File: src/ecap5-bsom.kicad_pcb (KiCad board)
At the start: 2 copper layers, 69.6 x 30 mm, 183 parts, among them J13 DDR4_SODIMM_Board, U1 L6981NDR, U10 IS42S16160J-*BL, U11 IS43DR86400E, U12 ASFC4G31M-51*, U2 L6981NDR, U3 ST1S41PHR, U4 L6981NDR, U5 LM3880MF*-1AA, U6 LFE5U-85F-*BG756*, U7 XLH335040.000000I, U8 W25Q128JVPIQ, U9 IS61WV25616BLL-*BLI

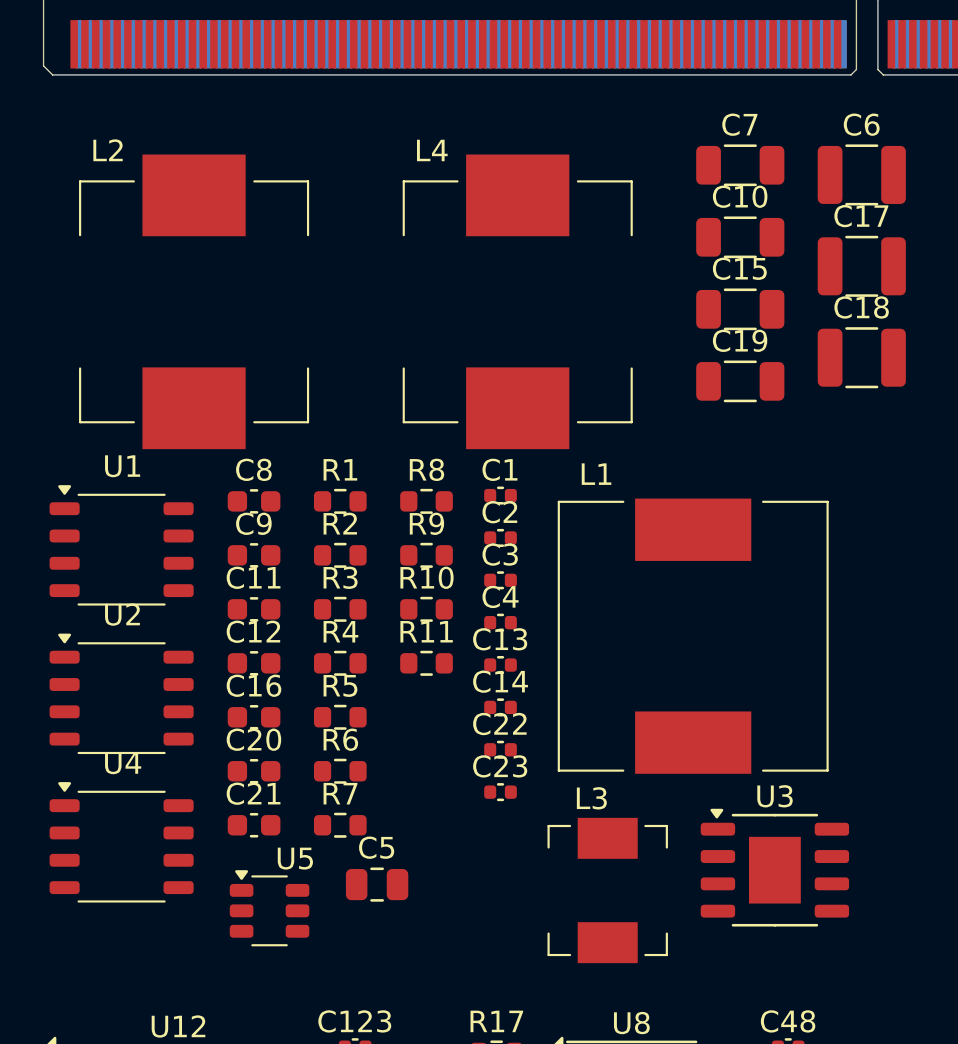
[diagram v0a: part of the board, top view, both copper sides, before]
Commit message: Update big inductors for smaller ones
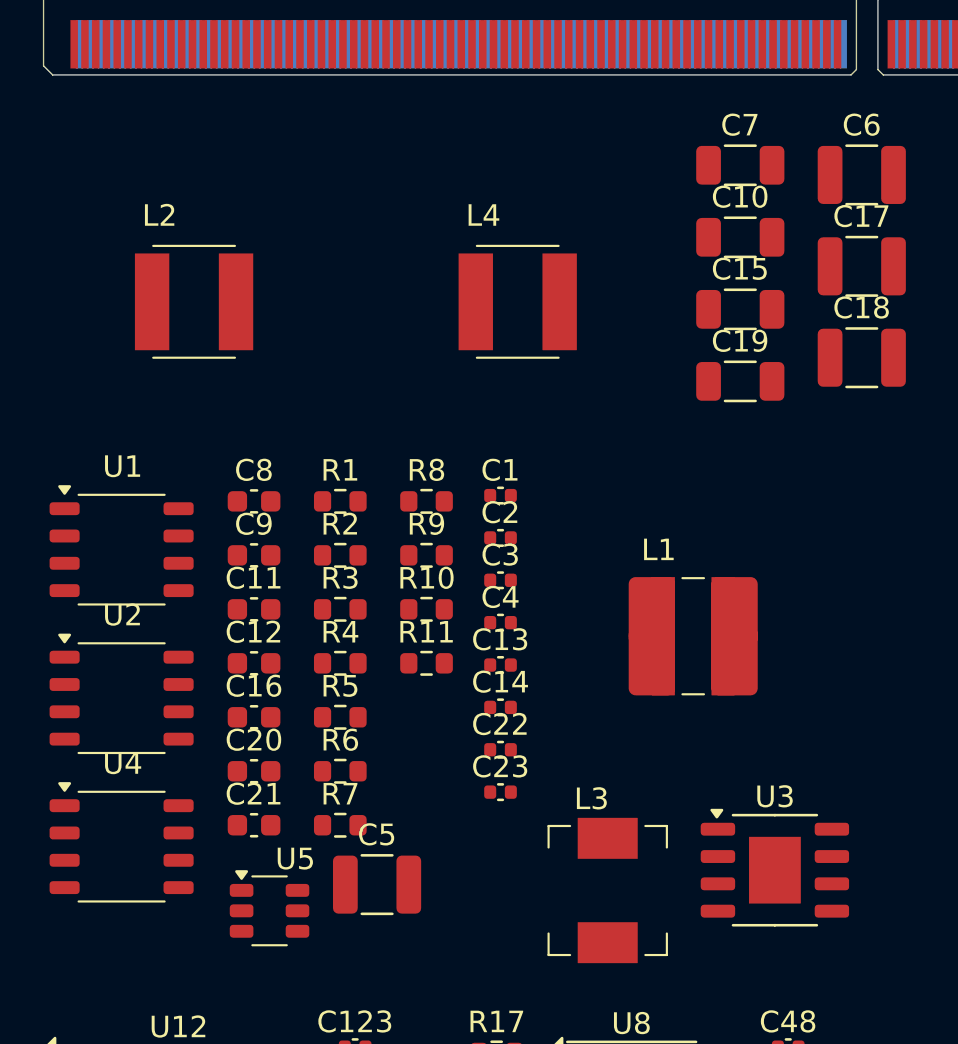
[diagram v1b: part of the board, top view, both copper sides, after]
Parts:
- C5: footprint Capacitor_SMD:C_0805_2012Metric -> Capacitor_SMD:C_1210_3225Metric
- L1: footprint ECAP5-DPROC:744770127 -> ECAP5-DPROC:744774127
- L2, L4: footprint ECAP5-DPROC:ETQ-P5M220YFC -> ECAP5-DPROC:74404052220

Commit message: Add remaining footprints
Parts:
- removed C17: 47u, Capacitor_SMD:C_1210_3225Metric
- removed C18: 100u, Capacitor_SMD:C_1210_3225Metric
- removed C19: 10u, Capacitor_SMD:C_1206_3216Metric
- removed C20, C21: 1u, Capacitor_SMD:C_0603_1608Metric
- removed R1: 237k 1%, Resistor_SMD:R_0603_1608Metric
- removed R2: 160k 1%, Resistor_SMD:R_0603_1608Metric
- removed R3: 82k 1%, Resistor_SMD:R_0603_1608Metric
- removed R4: 82.5k 1%, Resistor_SMD:R_0603_1608Metric
- added R30: 21k 1%, Resistor_SMD:R_0402_1005Metric, F.Cu at (160.7, 76.6)
- added R31: 10k 1%, Resistor_SMD:R_0402_1005Metric, F.Cu at (160.7, 78.6)
- added R33: 30.9k 1%, Resistor_SMD:R_0402_1005Metric, F.Cu at (160.7, 80.6)
- added R34: 10k 1%, Resistor_SMD:R_0402_1005Metric, F.Cu at (160.7, 82.6)
- C1, C2: value 100n -> 22u; footprint Capacitor_SMD:C_0402_1005Metric -> Capacitor_SMD:C_0805_2012Metric
- C10, C7: value 10u -> 100n; footprint Capacitor_SMD:C_1206_3216Metric -> Capacitor_SMD:C_0603_1608Metric
- C11: value 1u -> 100n; footprint Capacitor_SMD:C_0603_1608Metric -> Capacitor_SMD:C_0402_1005Metric
- C12, C16: value 1u -> 22u; footprint Capacitor_SMD:C_0603_1608Metric -> Capacitor_SMD:C_0805_2012Metric
- C13: value 100n -> 10u; footprint Capacitor_SMD:C_0402_1005Metric -> Capacitor_SMD:C_0805_2012Metric
- C14: value 62p -> 100n; footprint Capacitor_SMD:C_0402_1005Metric -> Capacitor_SMD:C_0603_1608Metric
- C15: value 10u -> 100n; footprint Capacitor_SMD:C_1206_3216Metric -> Capacitor_SMD:C_0402_1005Metric
- C3: value 18p -> 10u; footprint Capacitor_SMD:C_0402_1005Metric -> Capacitor_SMD:C_0805_2012Metric
- C4: value 47p -> 100n
- C5: value 47u -> 100n; footprint Capacitor_SMD:C_1210_3225Metric -> Capacitor_SMD:C_0603_1608Metric
- C6: value 100u -> 10u; footprint Capacitor_SMD:C_1210_3225Metric -> Capacitor_SMD:C_0805_2012Metric
- C8: value 1u -> 100n
- C9: value 1u -> 10u; footprint Capacitor_SMD:C_0603_1608Metric -> Capacitor_SMD:C_0805_2012Metric
- L1: value 27u -> 1u; footprint ECAP5-DPROC:744774127 -> ECAP5-DPROC:Bourns_SRN8040
- L2: value 22u -> 2.2u; footprint ECAP5-DPROC:74404052220 -> ECAP5-DPROC:Bourns_SRN6045
- L3: value 2.2u -> 3.3u; footprint ECAP5-DPROC:ETQ-P3M2R2KVP -> ECAP5-DPROC:Bourns_SRN6045
- L4: value 22u -> 3.3u; footprint ECAP5-DPROC:74404052220 -> ECAP5-DPROC:Bourns_SRN6045
- R10, R11, R9: footprint Resistor_SMD:R_0603_1608Metric -> Resistor_SMD:R_0402_1005Metric
- R5: value 8.2k 1% -> 8.25k 1%; footprint Resistor_SMD:R_0603_1608Metric -> Resistor_SMD:R_0402_1005Metric
- R6: value 91k 1% -> 12.4k 1%; footprint Resistor_SMD:R_0603_1608Metric -> Resistor_SMD:R_0402_1005Metric
- R7: value 22k 1% -> 10k 1%; footprint Resistor_SMD:R_0603_1608Metric -> Resistor_SMD:R_0402_1005Metric
- R8: value 82k 1% -> 10k 1%; footprint Resistor_SMD:R_0603_1608Metric -> Resistor_SMD:R_0402_1005Metric
- U1: value L6981NDR -> TPS565242DRDR; footprint ECAP5-DPROC:L6981 -> ECAP5-DPROC:TI_DRL0006A
- U2, U4: value L6981NDR -> TPS562202DRLR; footprint ECAP5-DPROC:L6981 -> ECAP5-DPROC:TI_DRL0006A
- U3: value ST1S41PHR -> TPS562202DRLR; footprint ECAP5-DPROC:ST1S41PHR -> ECAP5-DPROC:TI_DRL0006A
- moved C129 69.8 mm to (129.8, 120.5)
- moved C130 69.8 mm to (129.8, 122.4)
- moved C131 69.8 mm to (129.8, 124.4)
- moved D4 58.4 mm to (170.2, 122.6)
- moved D5 58.4 mm to (170.2, 125.2)
- moved R27 58.4 mm to (174.2, 120.0)
- moved R28 58.4 mm to (174.2, 122.5)
- moved R29 58.4 mm to (174.2, 125.0)
- moved D3 58.4 mm to (170.2, 120.0)
- moved C5 57.3 mm to (154.3, 74.9)
- moved R7 57.1 mm to (157.8, 78.6)
- moved R6 56.8 mm to (157.8, 76.6)
- moved R5 56.5 mm to (157.8, 74.6)
- moved U2 56.3 mm to (150.5, 78.9)
- moved U4 56.2 mm to (150.5, 86.0)
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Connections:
- C1 pad 1: Net-(U1-SW) -> +1V1
- C1 pad 2: Net-(U1-BOOT) -> GND
- C11 pad 1: VIN9_15 -> Net-(U3-BST)
- C11 pad 2: GND -> Net-(U3-SW)
- C12 pad 1: Net-(U2-VCC) -> +2V5
- C13 pad 1: Net-(U4-SW) -> VIN9_15
- C13 pad 2: Net-(U4-BOOT) -> GND
- C14 pad 1: Net-(U4-VOUT/FB) -> VIN9_15
- C14 pad 2: +1V8 -> GND
- C15 pad 1: VIN9_15 -> Net-(U4-BST)
- C15 pad 2: GND -> Net-(U4-SW)
- C16 pad 1: VIN9_15 -> +3V3
- C2 pad 1: Net-(U2-SW) -> +1V8
- C2 pad 2: Net-(U2-BOOT) -> GND
- C3 pad 1: Net-(U1-VOUT/FB) -> VIN9_15
- C3 pad 2: +3V3 -> GND
- C4 pad 2: +2V5 -> Net-(U2-SW)
- C5 pad 1: +3V3 -> VIN9_15
- C6 pad 1: +2V5 -> VIN9_15
- C7 pad 1: VIN9_15 -> +1V1
- C9 pad 1: Net-(U1-VCC) -> VIN9_15
- L1 pad 2: +3V3 -> +1V1
- L2 pad 2: +2V5 -> +1V8
- L3 pad 2: +1V1 -> +2V5
- L4 pad 2: +1V8 -> +3V3
- R5 pad 2: Net-(U3-FB) -> Net-(U1-FB)
- R6 pad 2: Net-(U4-VOUT/FB) -> Net-(U2-FB)
- R7 pad 1: Net-(U3-FB) -> Net-(U1-FB)
- R8 pad 1: Net-(U4-VOUT/FB) -> Net-(U2-FB)
- U1 pad 1: Net-(U1-SW) -> VIN9_15
- U1 pad 2: Net-(U1-BOOT) -> Net-(U1-SW)
- U1 pad 3: Net-(U1-VCC) -> GND
- U1 pad 4: Net-(U1-VOUT/FB) -> GND
- U1 pad 5: VIN9_15 -> /Power/en_1v1
- U1 pad 6: GND -> Net-(U1-FB)
- U2 pad 1: Net-(U2-SW) -> VIN9_15
- U2 pad 2: Net-(U2-BOOT) -> Net-(U2-SW)
- U2 pad 3: Net-(U2-VCC) -> GND
- U2 pad 5: /Power/en_2v5 -> /Power/en_1v8
- U2 pad 6: GND -> Net-(U2-FB)
- U3 pad 2: /Power/en_1v1 -> Net-(U3-SW)
- U3 pad 3: Net-(U3-FB) -> GND
- U3 pad 4: GND -> Net-(U3-BST)
- U3 pad 5: unconnected-(U3-NC-Pad5) -> /Power/en_2v5
- U3 pad 6: VIN9_15 -> Net-(U3-FB)
- U4 pad 1: Net-(U4-SW) -> VIN9_15
- U4 pad 2: Net-(U4-BOOT) -> Net-(U4-SW)
- U4 pad 3: Net-(U4-VCC) -> GND
- U4 pad 4: Net-(U4-VOUT/FB) -> Net-(U4-BST)
- U4 pad 5: /Power/en_1v8 -> VIN9_15
- U4 pad 6: GND -> Net-(U4-FB)
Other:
- outline, holes or cut-outs redrawn

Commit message: Define the board stackup and netclasses (#86)
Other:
- copper layers 2 -> 6

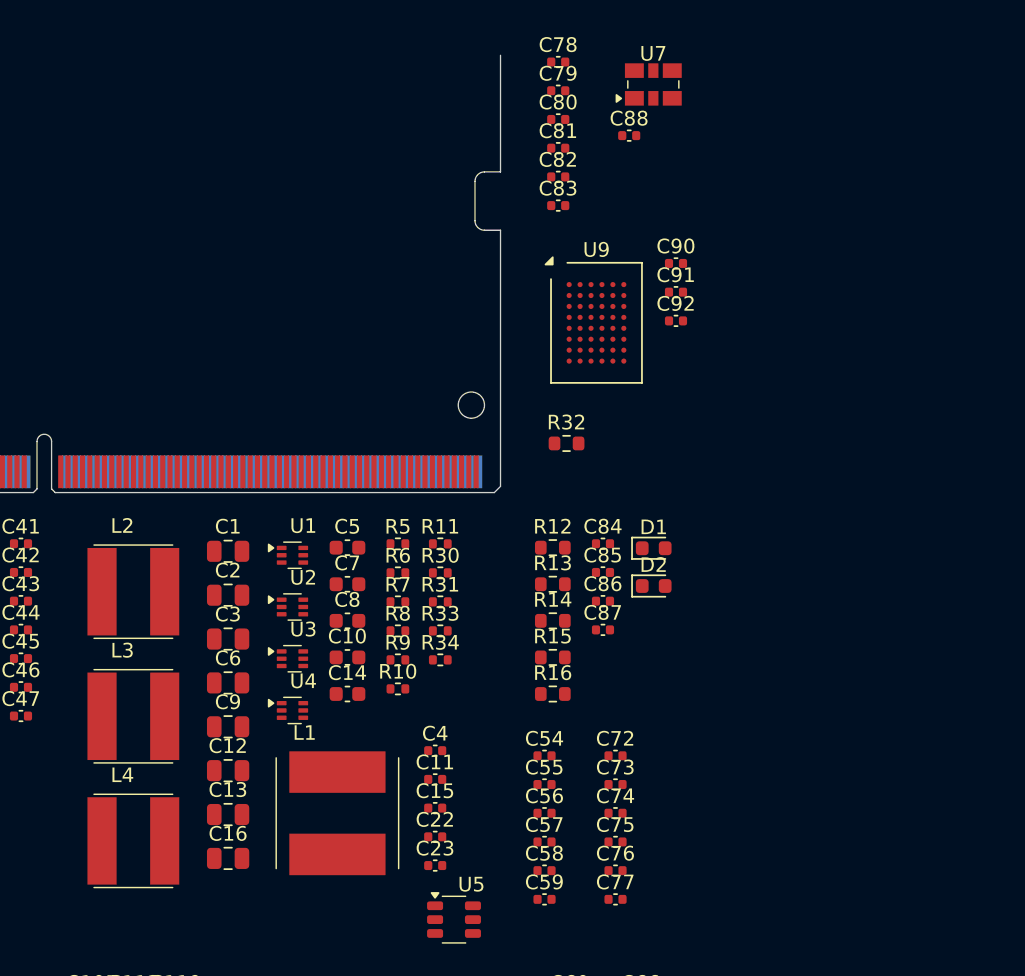
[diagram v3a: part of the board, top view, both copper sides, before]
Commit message: Replaces the inductors for smaller ones
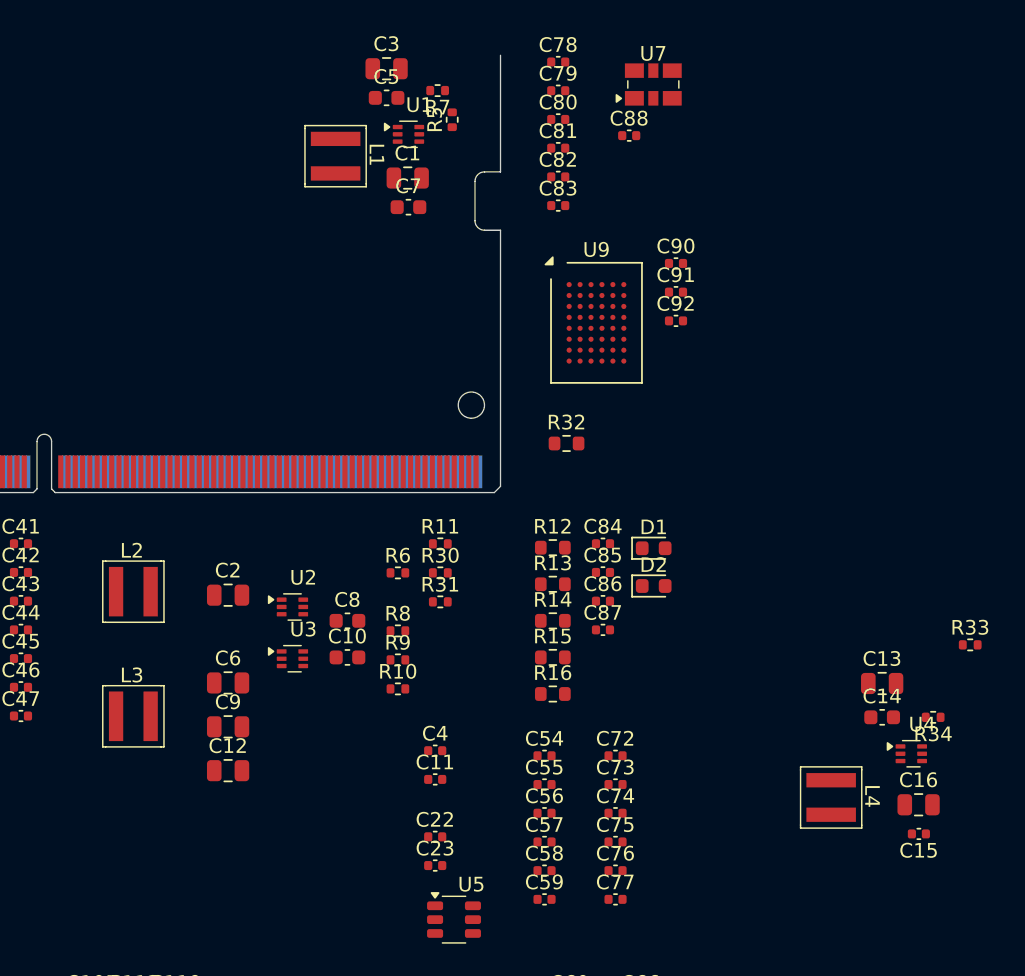
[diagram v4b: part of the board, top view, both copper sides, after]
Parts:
- L1: footprint ECAP5-DPROC:Bourns_SRN8040 -> ECAP5-DPROC:Coilcraft_XAL4020
- L2: footprint ECAP5-DPROC:Bourns_SRN6045 -> ECAP5-DPROC:Coilcraft_XAL4020
- L3, L4: footprint ECAP5-DPROC:Bourns_SRN6045 -> ECAP5-DPROC:Coilcraft_XAL4030
- moved L4 48.0 mm to (187.5, 92.0), turned to -90 degrees
- moved C16 47.5 mm to (193.5, 92.5)
- moved C13 45.8 mm to (191.0, 84.2)
- moved L1 45.1 mm to (153.5, 48.0), turned to -90 degrees
- moved U4 42.6 mm to (193.0, 89.0)
- moved C3 40.6 mm to (157.0, 42.0)
- moved C14 36.7 mm to (191.0, 86.5)
- moved R33 36.4 mm to (197.0, 81.5)
- moved R7 35.2 mm to (160.5, 43.5), turned to 180 degrees
- moved R34 34.0 mm to (194.5, 86.5), turned to 180 degrees
- moved C15 33.2 mm to (193.5, 94.5), turned to 180 degrees
- moved C5 31.0 mm to (157.0, 44.0)
- moved U1 30.0 mm to (158.5, 46.5)
- moved R5 29.3 mm to (161.5, 45.5), turned to 90 degrees
- moved C1 28.4 mm to (158.4, 49.5)
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
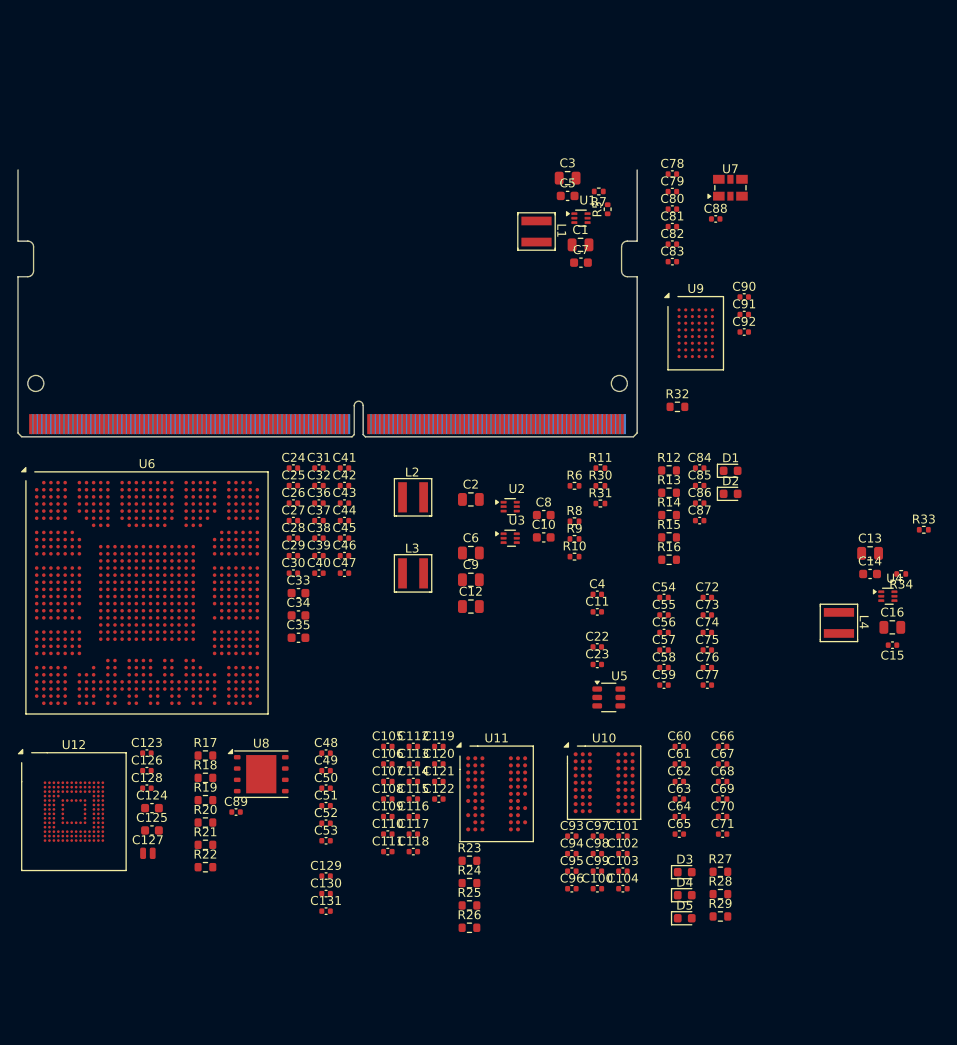
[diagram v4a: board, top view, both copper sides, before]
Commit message: Starts routing the power supply
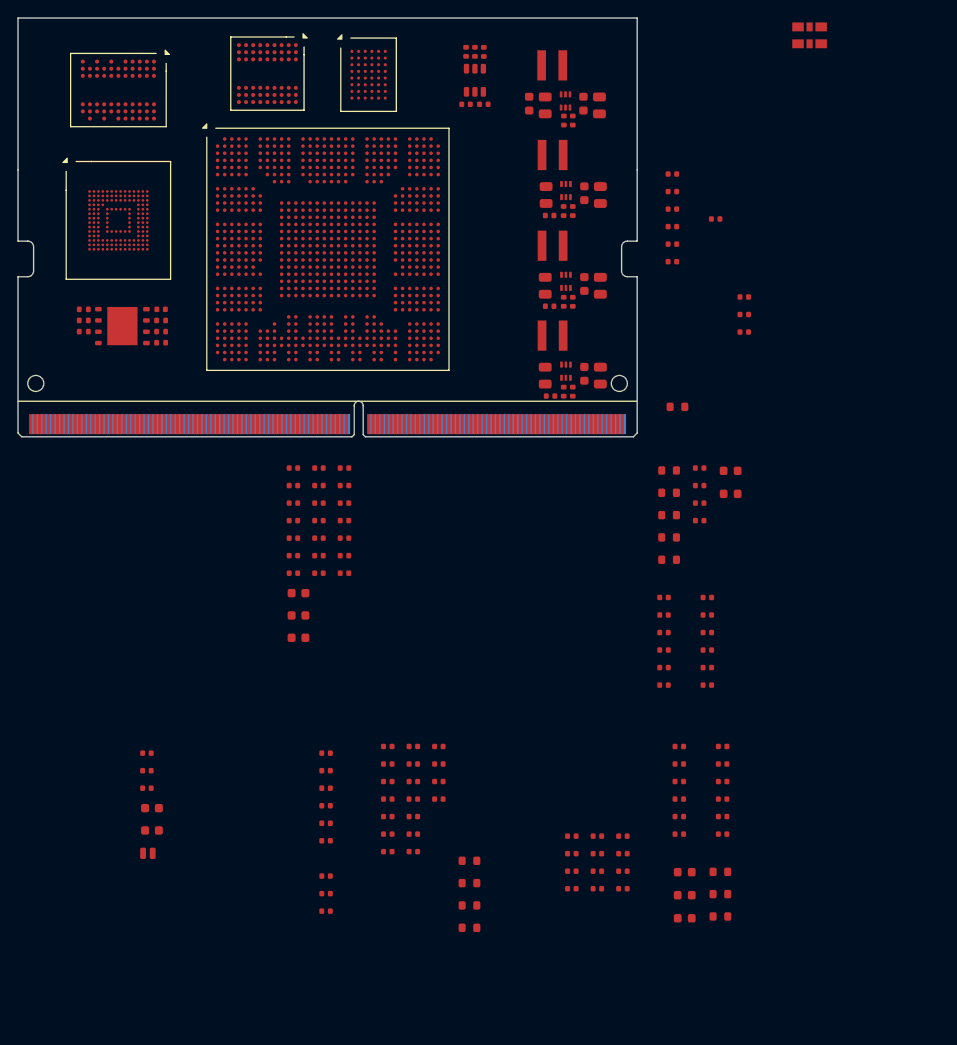
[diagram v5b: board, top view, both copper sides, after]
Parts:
- R17, R18, R19, R20, R21, R22: footprint Resistor_SMD:R_0603_1608Metric -> Resistor_SMD:R_0402_1005Metric
- moved U11 89.8 mm to (106.5, 32.1), turned to -90 degrees
- moved U10 88.2 mm to (123.2, 30.2), turned to -90 degrees
- moved U5 71.0 mm to (146.6, 31.0), turned to 90 degrees
- moved U12 66.7 mm to (106.5, 46.8)
- moved C23 64.2 mm to (147.6, 33.7)
- moved C22 62.8 mm to (145.6, 33.7)
- moved R21 61.7 mm to (102.6, 56.8), turned to 180 degrees
- moved R22 60.4 mm to (111.3, 59.2)
- moved R10 57.8 mm to (146.6, 27.8), turned to -90 degrees
- moved C89 57.1 mm to (111.3, 56.8)
- moved R20 56.7 mm to (111.3, 58.0)
- moved R9 56.1 mm to (145.6, 27.8), turned to -90 degrees
- moved R19 54.4 mm to (102.6, 59.2), turned to 180 degrees
- moved R18 53.2 mm to (102.6, 58.0), turned to 180 degrees
- moved U8 52.7 mm to (107.0, 58.6)
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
